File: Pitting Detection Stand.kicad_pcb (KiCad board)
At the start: 2 copper layers, 21 parts, among them J1 Conn_01x02_Pin, J2 Conn_01x02_Pin, J3 Conn_01x02_Pin, J4 Screw_Terminal_01x02, M1 Nema 17 (Z-axis), M2 28BYJ-48 (X-axis), M3 28BYJ-48 (Y-axis), M4 Servo for focusing lense, SW1 U_Bound SW, SW2 U_Bound SW, SW3 U_Bound SW, SW4 U_Bound SW, SW5 U_Bound SW, SW6 U_Bound SW

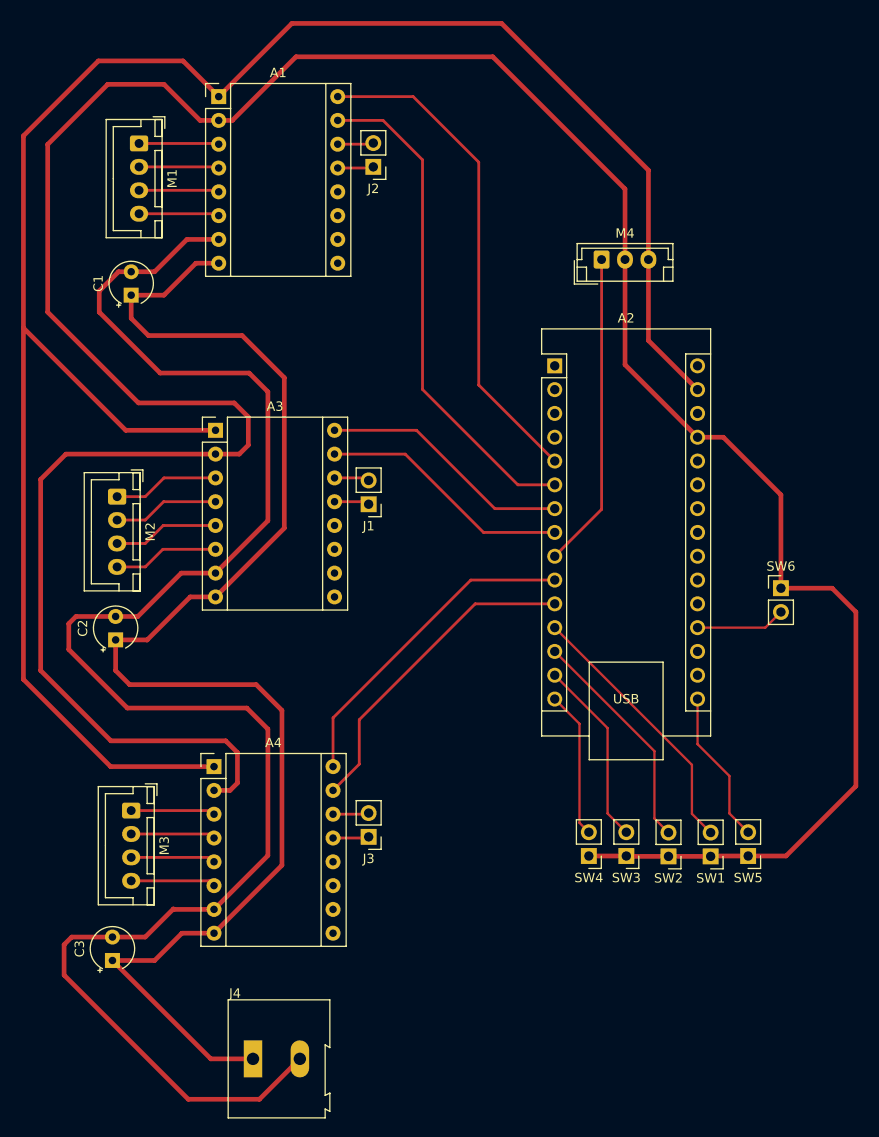
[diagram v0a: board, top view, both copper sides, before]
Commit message: Changed the route track width and added a ready to inkjet print pdf of the pcb board.
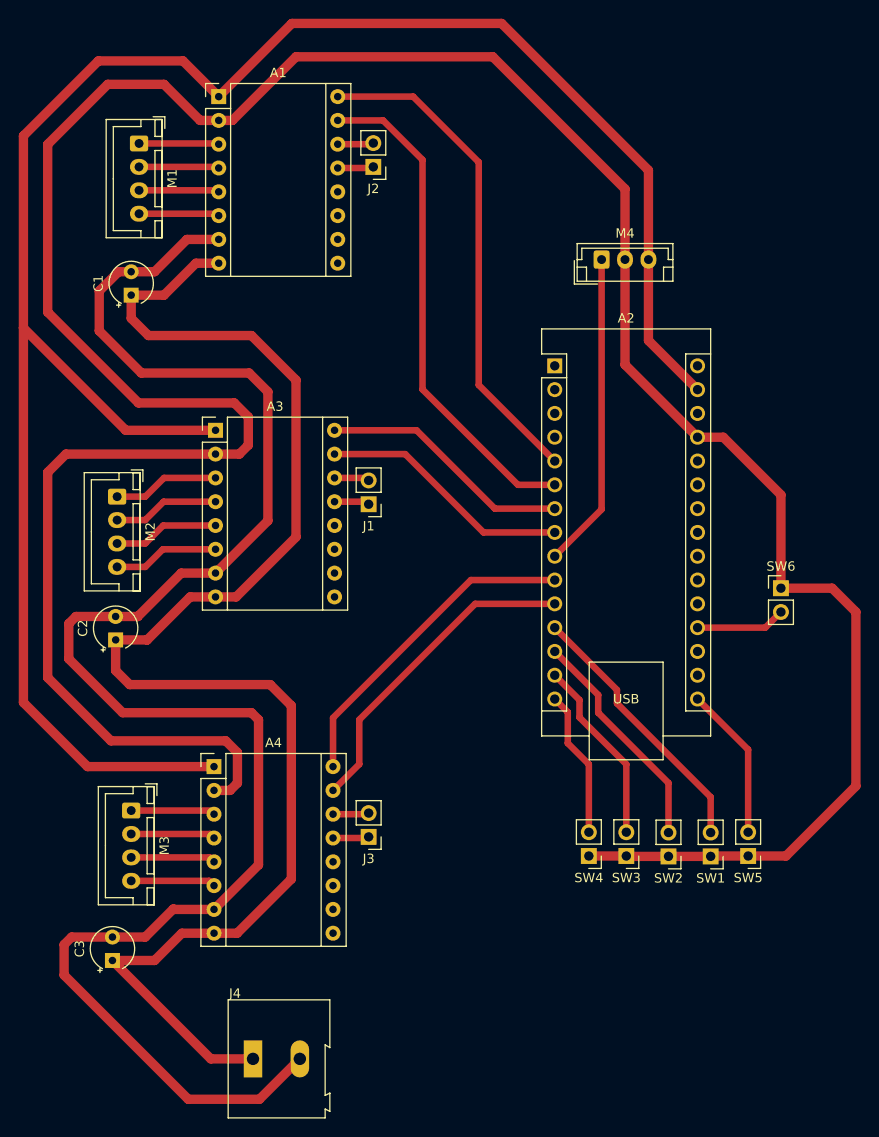
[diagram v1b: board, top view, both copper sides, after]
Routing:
- net +12V: track 152.1 -> 158.2 mm
- net GND: track 395.0 -> 397.4 mm
- net +5V: track 306.6 -> 306.0 mm
